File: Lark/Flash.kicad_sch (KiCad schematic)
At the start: 2 parts, among them U15 W25Q128JVSIQ

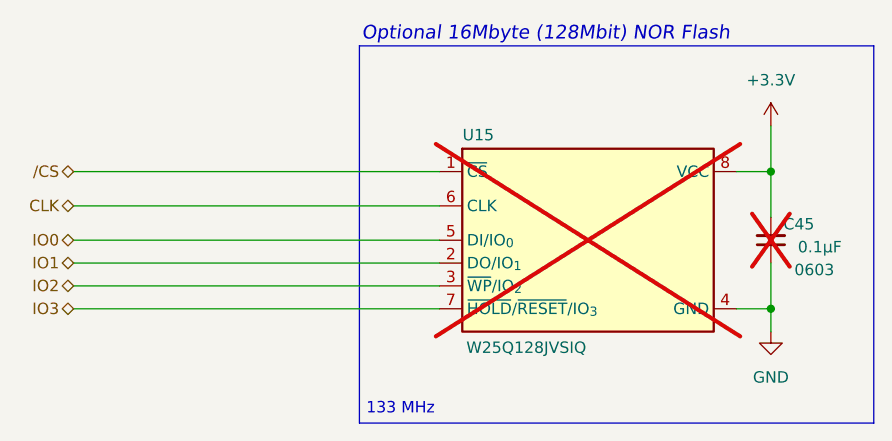
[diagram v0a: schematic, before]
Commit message: updated WIP
- fixed high-side switch (swapped out pfets)
- swapped out bleeder fet.
- changed a few footprints.
- changed zeners to 15v ones
- added soft-start cap back in to the high-side switch.

(today ive mainly been struggling with the inrush current, but I think its solved now)
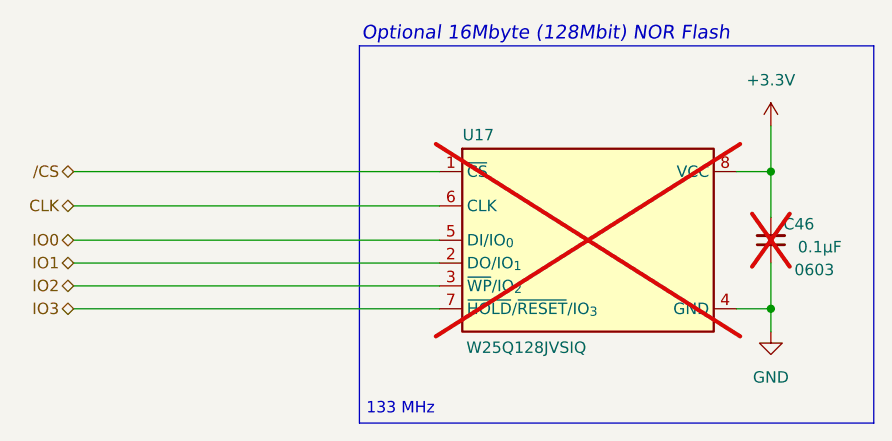
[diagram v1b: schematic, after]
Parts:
- renumbered C45 to C46, U15 to U17
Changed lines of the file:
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@@
 		(dnp no)
 		(fields_autoplaced yes)
-		(property "Reference" "#PWR0184"
+		(property "Reference" "#PWR0185"
 			(at 168.91 111.76 0)
 			(effects
@@
 			(project "Lark"
 				(path "/a351af57-4353-47da-9f45-7393de572768/510bbd44-ee11-40bc-952d-6cd0def4c817/fbf20d92-3dc5-48bd-8ff0-5e0b8683d6ab"
-					(reference "#PWR0184")
+					(reference "#PWR0185")
 					(unit 1)
 				)
@@
 		(dnp no)
 		(fields_autoplaced yes)
-		(property "Reference" "#PWR0183"
+		(property "Reference" "#PWR0184"
 			(at 168.91 86.36 0)
 			(effects
@@
 			(project "Lark"
 				(path "/a351af57-4353-47da-9f45-7393de572768/510bbd44-ee11-40bc-952d-6cd0def4c817/fbf20d92-3dc5-48bd-8ff0-5e0b8683d6ab"
-					(reference "#PWR0183")
+					(reference "#PWR0184")
 					(unit 1)
 				)
@@
 		(on_board yes)
 		(dnp yes)
-		(property "Reference" "U15"
+		(property "Reference" "U17"
 			(at 136.398 83.566 0)
 			(effects
@@
 			(project ""
 				(path "/a351af57-4353-47da-9f45-7393de572768/510bbd44-ee11-40bc-952d-6cd0def4c817/fbf20d92-3dc5-48bd-8ff0-5e0b8683d6ab"
-					(reference "U15")
+					(reference "U17")
 					(unit 1)
 				)
@@
 		(on_board yes)
 		(dnp yes)
-		(property "Reference" "C45"
+		(property "Reference" "C46"
 			(at 173.736 93.472 0)
 			(effects
@@
 			(project "Lark"
 				(path "/a351af57-4353-47da-9f45-7393de572768/510bbd44-ee11-40bc-952d-6cd0def4c817/fbf20d92-3dc5-48bd-8ff0-5e0b8683d6ab"
-					(reference "C45")
-					(unit 1)
-				)
+					(reference "C46")
+					(unit 1)
+				)

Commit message: Changed revision again...
- It dawned on me that this is rev 2, so the rev is now 01.00.1.
- Added thermal relief to the TH pads so I can actually solder the parts.
- Added more silkscreen to denote the rev, the github link, and ESD sensitivity of the device.
- Made minor pcb changes, I moved a test point, and cleaned up some traces.
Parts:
- C46, U17: now left out of the parts list
